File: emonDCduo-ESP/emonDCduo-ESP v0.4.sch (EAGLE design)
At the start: 78 parts, among them Q1 16Mhz XT49M-2016M, U1_TQFP ATMEGA328P

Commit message: RFM69 onto board
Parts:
- removed T3: (no value), con-weidmueller-sl35:180-2
- added ANT1: (no value), discrete:ANTENNA
- added C16, C19: 22pF, rcl:C-EUC0603
- added C2: 100nF, rcl:C-EUC0603
- added C20: tune, rcl:C-EUC0603
- added J$1: SMA_EDGE, SparkFun-Connectors:SMA_EDGE
- added R24: 120K, rcl:R-EU_R0603
- added RF: RFM12B, JeeParts:RFM12B
- C3: value 470UF -> 470uF
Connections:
- new net DIG1: C16.1, C19.1, C20.1, RF.ANT
- new net N$11: ANT1.1, C16.2
- new net N$24: C19.2, J$1.SIGNAL
- net 3.3V: now also C2.1, R24.2, RF.VCC
- net D10: now also R24.1, RF.SEL
- net D11/MOSI: now also RF.SDI
- net D12/MISO: now also RF.SDO
- net D13/SCK: now also RF.SCK
- net D2: now also RF.IRQ
- net GND: now also C2.2, C20.2, J$1.GND@0, J$1.GND@1, J$1.GND@2, J$1.GND@3, RF.GND; no longer T3.1, T3.2
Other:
- note added: "4.7V AFTER DIODE TO 3.3V"
- note added: "RFM12B RFM69CW"
- moved on the sheet: C21, C22, FTDI1, GPIO0, R17, R18, R19, R3, R6, R7, RX, TX

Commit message: DRC edited
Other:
- note added: "emonDC v0.4 : based on emonTx v3.4 by Glyn Hudson and Trystan Lea OpenEnergyMonitor.org"
- note removed: "emonDC v0.3 : based on emonTx v3.4 by Glyn Hudson and Trystan Lea OpenEnergyMonitor.org"
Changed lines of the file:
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@@
 <sheet>
 <plain>
-<text x="-82.55" y="184.15" size="1.778" layer="97">emonDC v0.3 : based on emonTx v3.4 by Glyn Hudson and Trystan Lea
+<text x="-82.55" y="184.15" size="1.778" layer="97">emonDC v0.4 : based on emonTx v3.4 by Glyn Hudson and Trystan Lea
 OpenEnergyMonitor.org</text>
 <text x="-82.55" y="180.34" size="1.778" layer="97">Daniel Bates     Dec 2016</text>

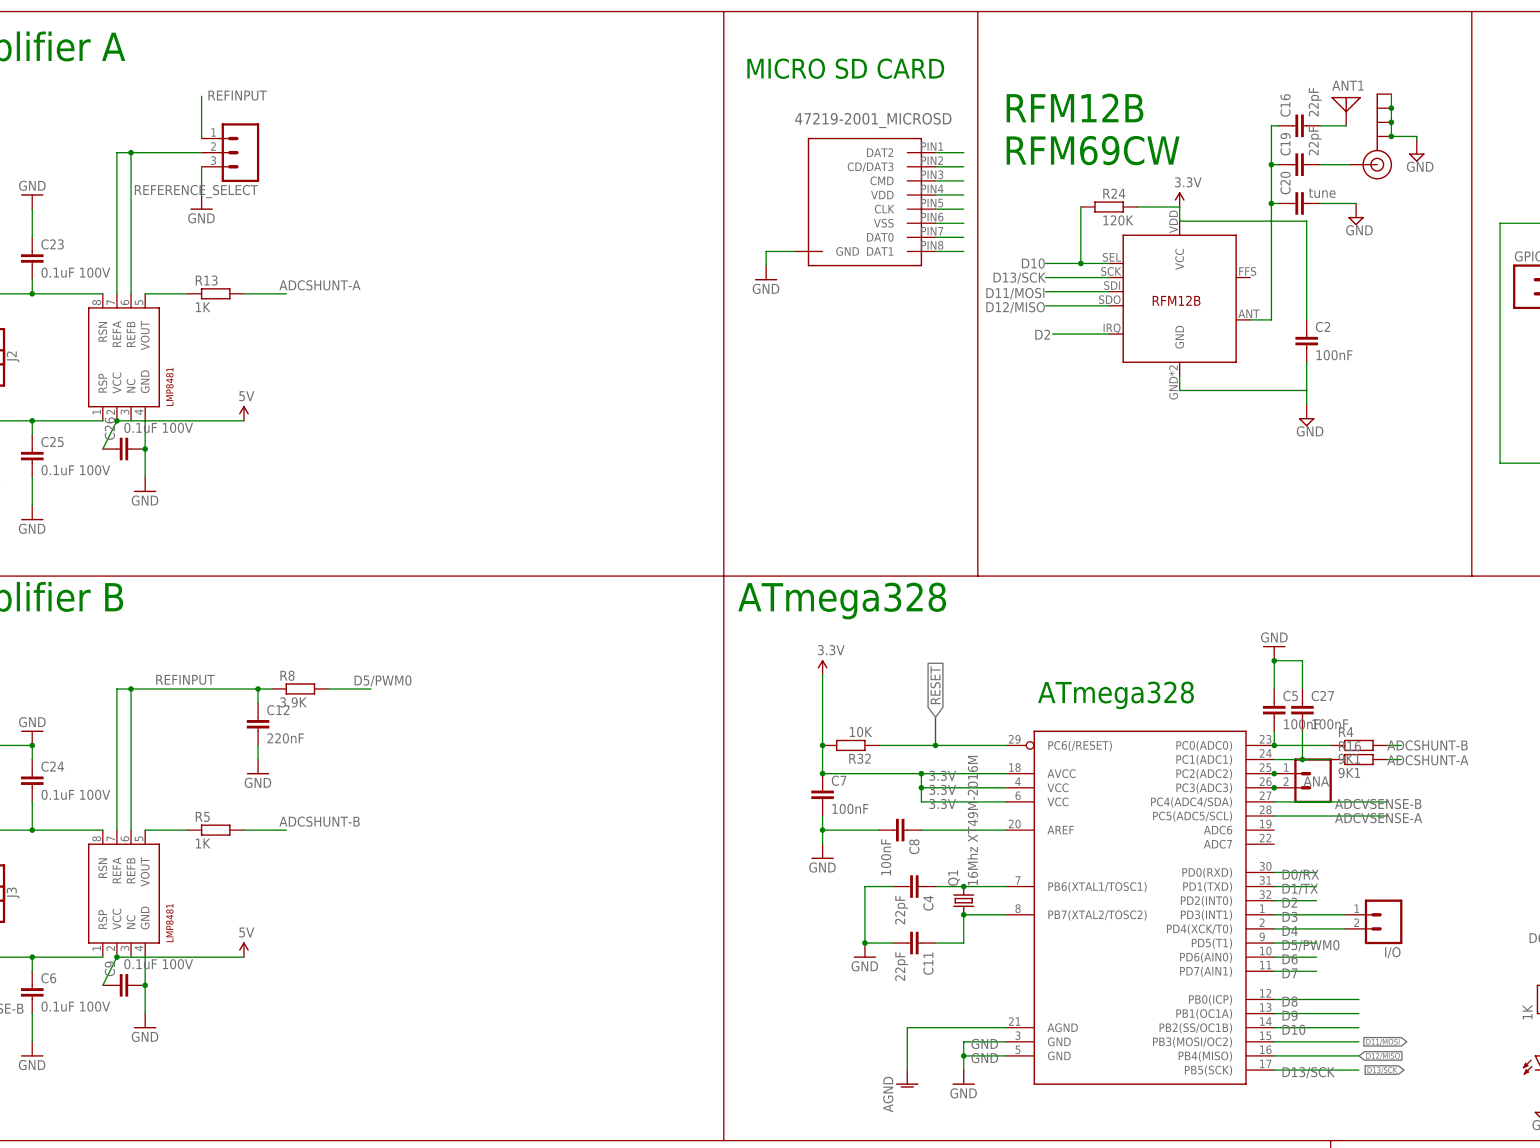
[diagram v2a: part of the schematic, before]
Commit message: antenna caps removed. camexport
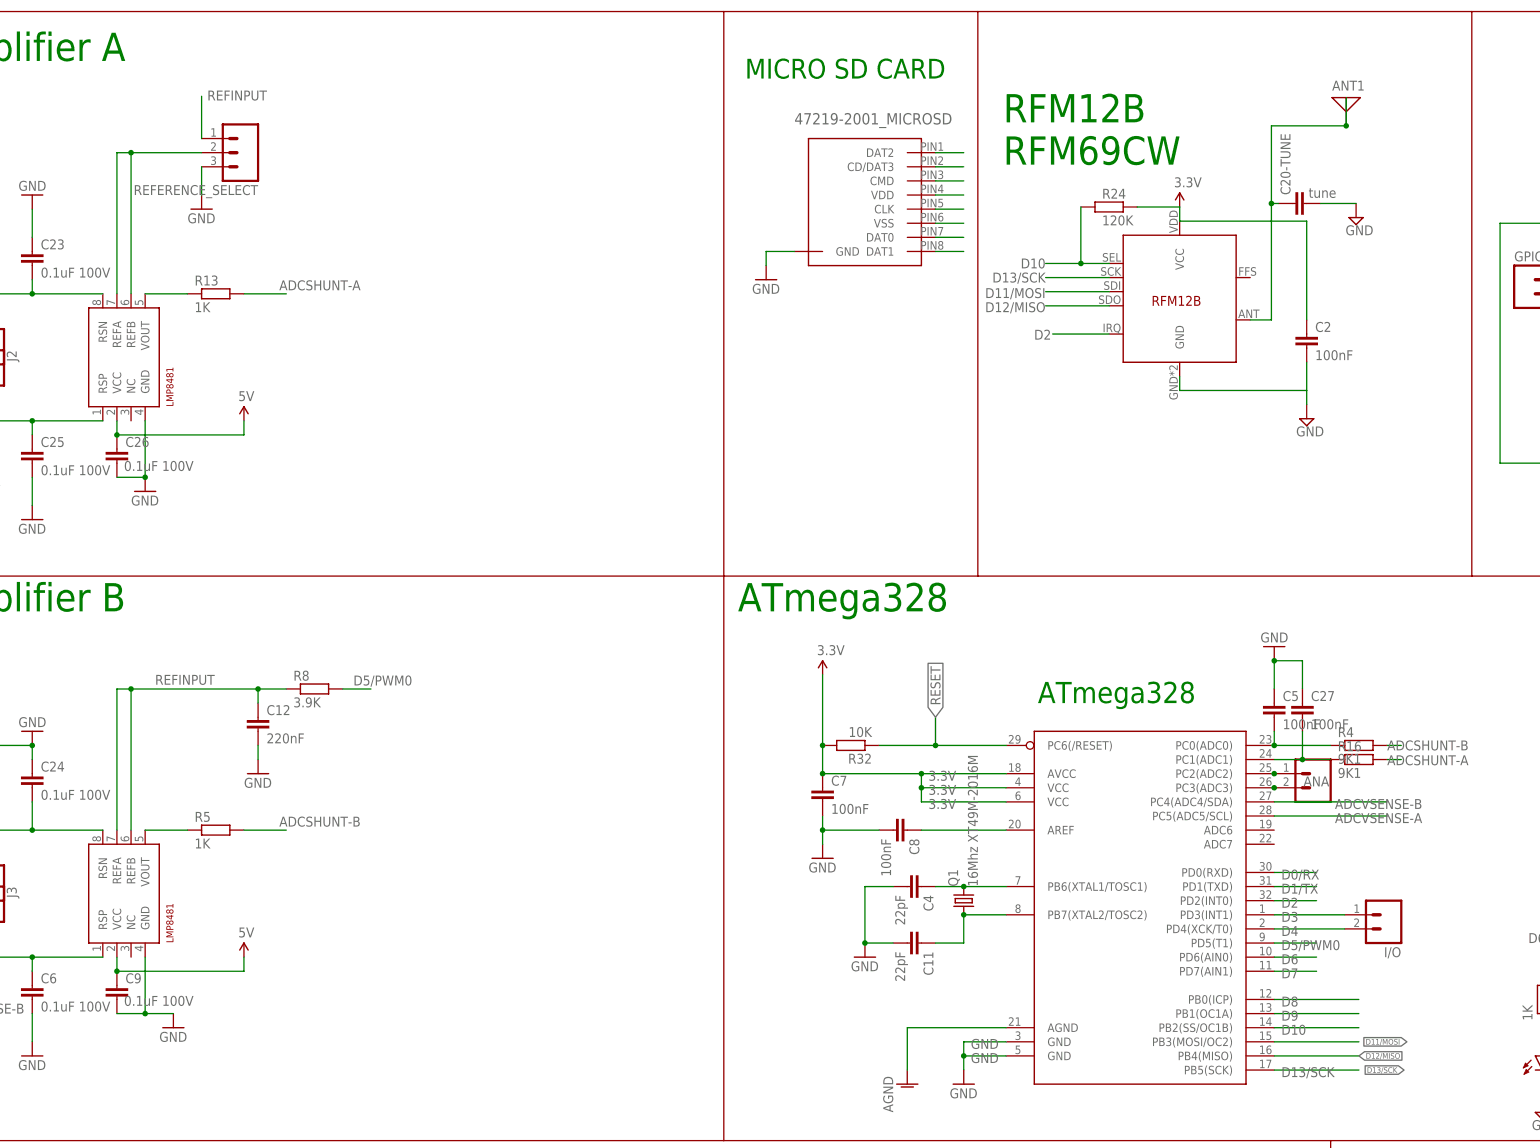
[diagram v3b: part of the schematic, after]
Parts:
- removed C16, C19: 22pF, rcl:C-EUC0603
- removed J$1: SMA_EDGE, SparkFun-Connectors:SMA_EDGE
- renumbered C20 to C20-TUNE
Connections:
- removed net N$11: ANT1.1, C16.2
- removed net N$24: C19.2, J$1.SIGNAL
- net DIG1: now also ANT1.1; no longer C16.1, C19.1
- net GND: no longer J$1.GND@0, J$1.GND@1, J$1.GND@2, J$1.GND@3
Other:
- moved on the sheet: C26, C9, R8

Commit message: gerber
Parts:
- added C19: 22pF, rcl:C-EUC0603
- added GPIO-4/5: (no value), SparkFun:M02PTH
- added PAD1: (no value), wirepad:SMD2
- renumbered C20-TUNE to C20/TUNE
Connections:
- new net N$3: ANT1.1, C19.2
- new net N$5: PAD1.P
- net DIG1: now also C19.1; no longer ANT1.1
- net GPIO4: now also GPIO-4/5.1
- net GPIO5: now also GPIO-4/5.2
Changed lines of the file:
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@@
 <setting verticaltext="up"/>
 </settings>
-<grid distance="0.1" unitdist="inch" unit="inch" style="lines" multiple="1" display="yes" altdistance="0.01" altunitdist="inch" altunit="inch"/>
+<grid distance="0.1" unitdist="inch" unit="inch" style="lines" multiple="1" display="no" altdistance="0.01" altunitdist="inch" altunit="inch"/>
 <layers>
 <layer number="1" name="Top" color="4" fill="1" visible="no" active="no"/>
@@
 <part name="SUPPLY2" library="supply2" deviceset="GND" device=""/>
 <part name="R24" library="rcl" deviceset="R-EU_" device="R0603" value="120K"/>
-<part name="C20-TUNE" library="rcl" deviceset="C-EU" device="C0603" value="tune"/>
+<part name="C20/TUNE" library="rcl" deviceset="C-EU" device="C0603" value="tune"/>
 <part name="SUPPLY6" library="supply2" deviceset="GND" device=""/>
 <part name="GND18" library="supply1" deviceset="0V" device="" value="GND"/>
+<part name="C19" library="rcl" deviceset="C-EU" device="C0603" value="22pF"/>
+<part name="PAD1" library="wirepad" deviceset="SMD2" device=""/>
+<part name="GPIO-4/5" library="SparkFun" deviceset="M02" device="PTH"/>
 </parts>
 <sheets>
@@
 <attribute name="VALUE" x="106.172" y="456.819" size="1.778" layer="96"/>
 </instance>
-<instance part="C20-TUNE" gate="G$1" x="140.462" y="460.756" smashed="yes" rot="R90">
+<instance part="C20/TUNE" gate="G$1" x="140.462" y="460.756" smashed="yes" rot="R90">
 <attribute name="NAME" x="140.081" y="462.28" size="1.778" layer="95" rot="R90"/>
 <attribute name="VALUE" x="148.336" y="463.55" size="1.778" layer="96" rot="R180"/>
@@
 <instance part="SUPPLY6" gate="GND" x="151.892" y="458.216"/>
 <instance part="GND18" gate="1" x="-121.92" y="231.14"/>
+<instance part="C19" gate="G$1" x="136.652" y="466.852" smashed="yes" rot="R180">
+<attribute name="NAME" x="135.128" y="466.471" size="1.778" layer="95" rot="R180"/>
+<attribute name="VALUE" x="133.858" y="474.726" size="1.778" layer="96" rot="R270"/>
+</instance>
+<instance part="PAD1" gate="1" x="147.32" y="467.36" rot="R90"/>
+<instance part="GPIO-4/5" gate="G$1" x="226.06" y="398.78" rot="R90"/>
 </instances>
 <busses>
@@
 </segment>
 <segment>
-<pinref part="C20-TUNE" gate="G$1" pin="2"/>
+<pinref part="C20/TUNE" gate="G$1" pin="2"/>
 <pinref part="SUPPLY6" gate="GND" pin="GND"/>
 <wire x1="151.892" y1="460.756" x2="145.542" y2="460.756" width="0.1524" layer="91"/>
@@
 <label x="203.2" y="444.5" size="1.778" layer="95"/>
 </segment>
+<segment>
+<pinref part="GPIO-4/5" gate="G$1" pin="2"/>
+<wire x1="223.52" y1="406.4" x2="223.52" y2="408.94" width="0.1524" layer="91"/>
+</segment>
 </net>
 <net name="GPIO4" class="0">
@@
 <wire x1="210.82" y1="441.96" x2="205.74" y2="441.96" width="0.1524" layer="91"/>
 <label x="203.2" y="441.96" size="1.778" layer="95"/>
+</segment>
+<segment>
+<pinref part="GPIO-4/5" gate="G$1" pin="1"/>
+<wire x1="226.06" y1="406.4" x2="226.06" y2="408.94" width="0.1524" layer="91"/>
 </segment>
 </net>
@@
 <net name="DIG1" class="0">
 <segment>
-<pinref part="C20-TUNE" gate="G$1" pin="1"/>
-<wire x1="150.114" y1="474.726" x2="136.652" y2="474.726" width="0.1524" layer="91"/>
-<wire x1="136.652" y1="474.726" x2="136.652" y2="460.756" width="0.1524" layer="91"/>
+<pinref part="C20/TUNE" gate="G$1" pin="1"/>
 <wire x1="136.652" y1="460.756" x2="136.652" y2="439.801" width="0.1524" layer="91"/>
 <wire x1="137.922" y1="460.756" x2="136.652" y2="460.756" width="0.1524" layer="91"/>
-<junction x="136.652" y="460.756"/>
 <pinref part="RF" gate="G$1" pin="ANT"/>
 <wire x1="132.842" y1="439.801" x2="136.652" y2="439.801" width="0.1524" layer="91"/>
+<pinref part="C19" gate="G$1" pin="1"/>
+<wire x1="136.652" y1="460.756" x2="136.652" y2="464.312" width="0.1524" layer="91"/>
+<junction x="136.652" y="460.756"/>
+</segment>
+</net>
+<net name="N$3" class="0">
+<segment>
 <pinref part="ANT1" gate="A" pin="1"/>
-<wire x1="150.114" y1="474.726" x2="150.114" y2="479.806" width="0.1524" layer="91"/>
-<junction x="150.114" y="474.726"/>
-</segment>
-</net>
+<wire x1="150.114" y1="474.726" x2="136.652" y2="474.726" width="0.1524" layer="91"/>
+<pinref part="C19" gate="G$1" pin="2"/>
+<wire x1="136.652" y1="474.726" x2="136.652" y2="471.932" width="0.1524" layer="91"/>
+</segment>
+</net>
+<net name="N$5" class="0">
+<segment>
+<pinref part="PAD1" gate="1" pin="P"/>
+<wire x1="147.32" y1="469.9" x2="152.4" y2="469.9" width="0.1524" layer="91"/>
+</segment>
+</net>

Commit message: refinement
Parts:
- I1: value (none) -> 330uH
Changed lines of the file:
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@@
 <attribute name="OC_FARNELL" value="2492609"/>
 </part>
-<part name="I1" library="SRR0603-331KL" deviceset="SRR0603-331KL" device="">
+<part name="I1" library="SRR0603-331KL" deviceset="SRR0603-331KL" device="" value="330uH">
 <attribute name="MF" value="BOURNS"/>
 <attribute name="MPN" value="SRR0603-331KL"/>
